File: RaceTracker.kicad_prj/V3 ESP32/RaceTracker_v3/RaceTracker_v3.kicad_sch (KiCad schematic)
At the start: 44 parts, among them J1 USB-C, J2 Battery, J3 Qwiic GPS (I2C), J4 microSD, J5 UART Debug, SW1 PWR, SW2 RESET, SW3 BOOT, U1 ESP32-S3-WROOM-1-N8, U2 MCP73831T-2ACI/OT, U3 AP2112K-3.3, U4 WSEN-ISDS

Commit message: V3: manuelle Schaltplan-Aenderungen committen
Co-Authored-By: Claude Sonnet 5 <noreply@anthropic.com>
Claude-Session: https://claude.ai/code/session_01KJ1x8W8LsYuDo52VfB14br
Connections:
- net GND: now also R1.1, R2.1; no longer R1.2, R2.2
- net at J1.B5 (CC2): now also R2.2; no longer R2.1
- net at J1.A5 (CC1): now also R1.2; no longer R1.1
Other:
- moved on the sheet: C1, C10, C2, C3, C4, C5, C6, C7, C8, C9, D2, D3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

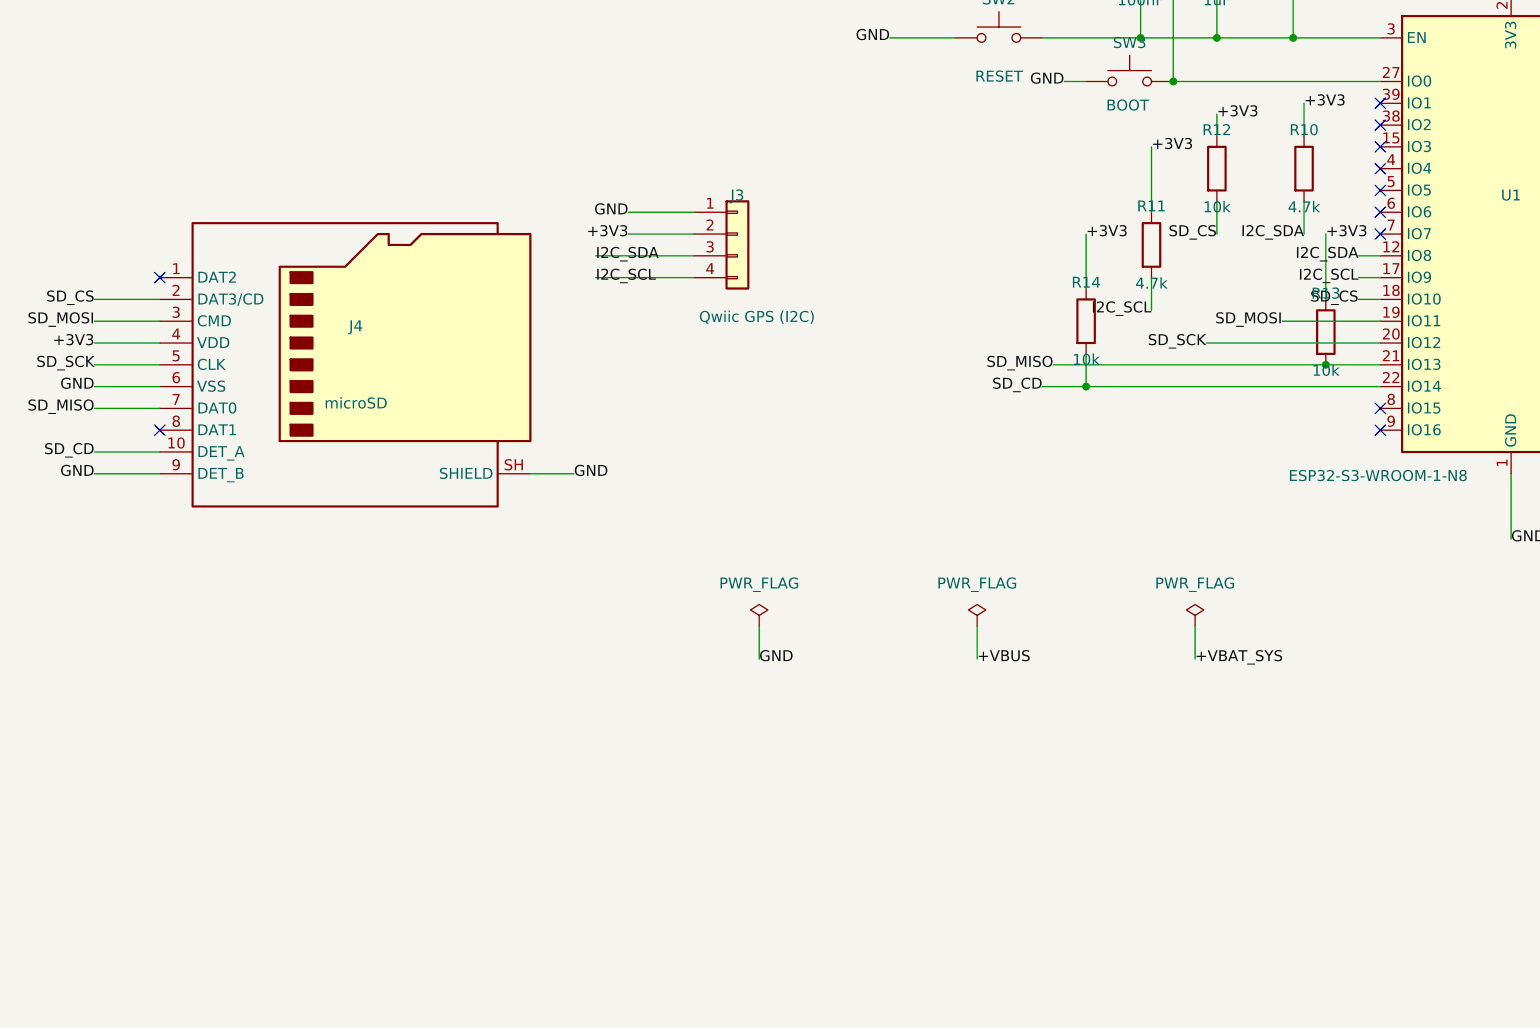
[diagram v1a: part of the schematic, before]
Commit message: V3: e-Paper Connector-Header (J6) ergaenzt
Co-Authored-By: Claude Sonnet 5 <noreply@anthropic.com>
Claude-Session: https://claude.ai/code/session_01KJ1x8W8LsYuDo52VfB14br
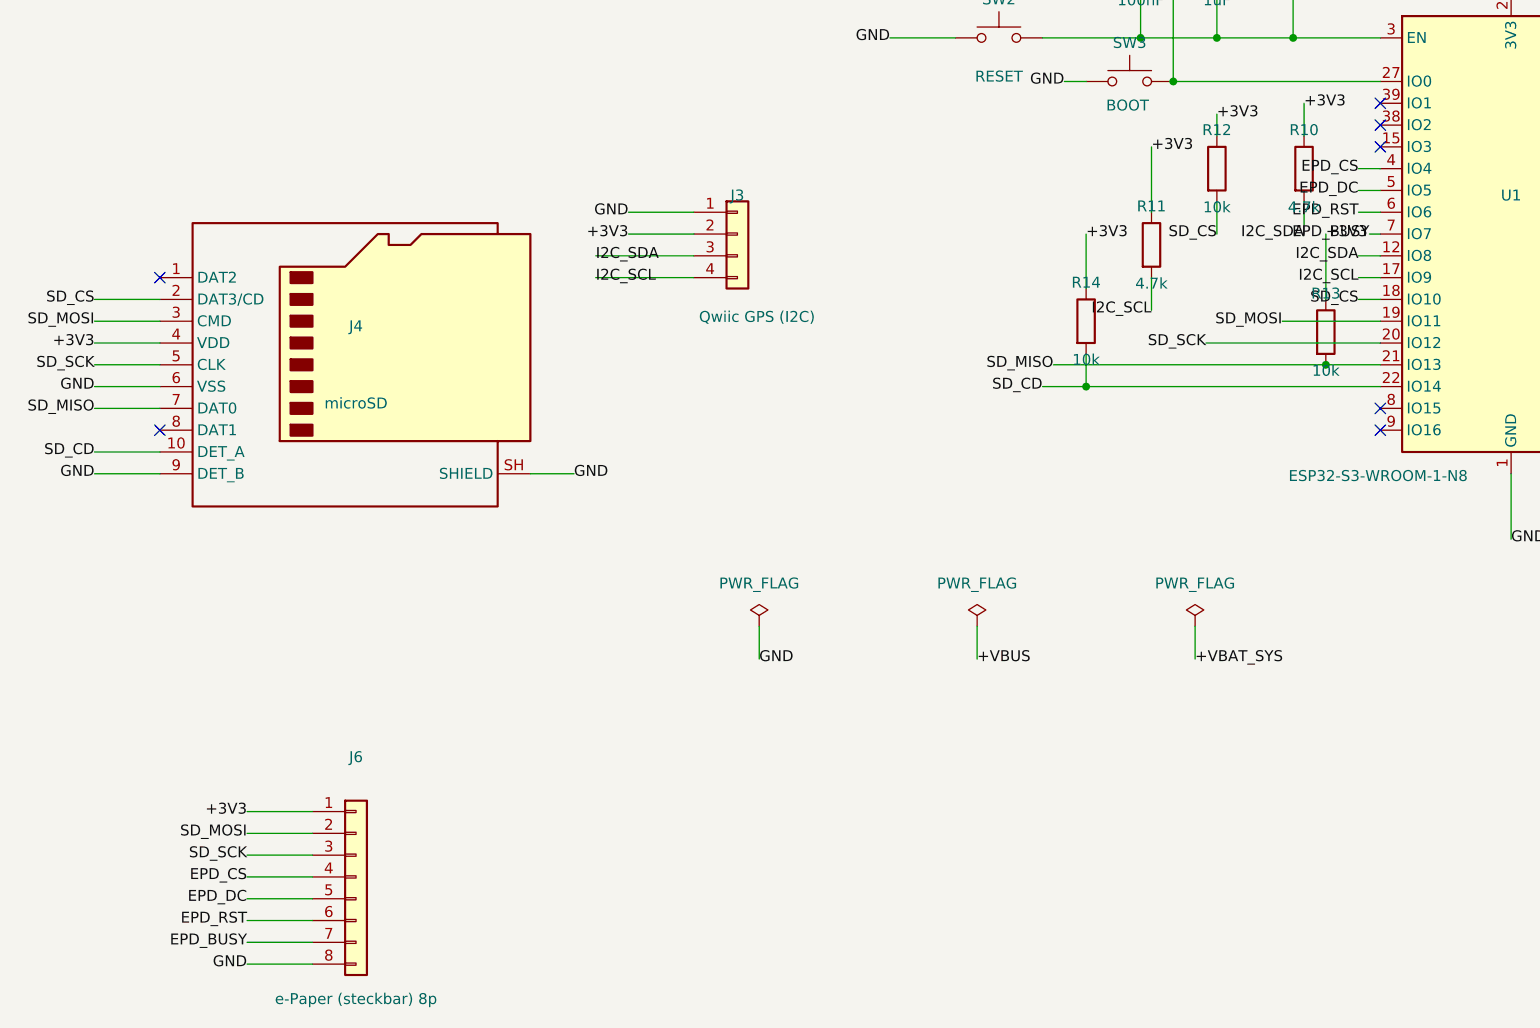
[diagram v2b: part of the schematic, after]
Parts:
- added J6: e-Paper (steckbar) 8p, Connector_PinHeader_2.54mm:PinHeader_1x08_P2.54mm_Vertical, symbol Connector_Generic:Conn_01x08
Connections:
- net +3V3: now also J6.1 (Pin_1)
- net GND: now also J6.8 (Pin_8)
- net SD_MOSI: now also J6.2 (Pin_2)
- net SD_SCK: now also J6.3 (Pin_3)
- net EPD_CS: now reaches U1.4 (IO4)
- net EPD_CS: now also J6.4 (Pin_4)
- net EPD_DC: now reaches U1.5 (IO5)
- net EPD_DC: now also J6.5 (Pin_5)
- net EPD_RST: now reaches U1.6 (IO6)
- net EPD_RST: now also J6.6 (Pin_6)
- net EPD_BUSY: now reaches U1.7 (IO7)
- net EPD_BUSY: now also J6.7 (Pin_7)
- no-connect marks 31 -> 27

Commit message: V3: C8-Plane-Via, J3 zur Steckerleiste, Pin-Beschriftung
- C8: fehlenden /+3V3-Stitching-Via ergaenzt (GND-Pad hatte schon einen
  passenden Via in Reichweite, kein neuer noetig)
- J3 (Qwiic GPS I2C) von JST-SH auf 2.54mm-Stiftleiste
  (PinHeader_1x04_P2.54mm_Vertical) umgestellt - das reale SparkFun-
  Modul hat dafuer eine eigene PTH-Stiftleiste mit identischer
  Pinbelegung (GND/VCC/SDA/SCL), verifiziert gegen das Datenblatt im
  Repo-Root. Schaltplan-Footprint-Feld + PCB-Footprint getauscht,
  Position/Netze erhalten. Feinplatzierung macht der User selbst.
- Pin-Funktions-Beschriftung (Silk) fuer alle 3 Stiftleisten-Header
  J3/J5/J6 ergaenzt (GND/3V3/SDA/SCL, RXD/TXD, 3V3/MOSI/SCK/CS/DC/
  RST/BUSY/GND), 0.8mm Texthoehe, damit beim Verkabeln nichts
  vertauscht wird

Verifiziert: kicad-cli pcb drc --severity-all -> 0 Errors (nur 5
erwartete lib_footprint_mismatch-Warnings + 4 via_dangling/2
unconnected von J3s alter JST-Position, die der User beim
Neuplatzieren mit aufraeumt). ERC weiterhin 0/0.

Co-Authored-By: Claude Sonnet 5 <noreply@anthropic.com>
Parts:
- J3: footprint Connector_JST:JST_SH_SM04B-SRSS-TB_1x04-1MP_P1.00mm_Horizontal -> Connector_PinHeader_2.54mm:PinHeader_1x04_P2.54mm_Vertical
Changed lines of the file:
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@@
 			)
 		)
-		(property "Footprint" "Connector_JST:JST_SH_SM04B-SRSS-TB_1x04-1MP_P1.00mm_Horizontal"
+		(property "Footprint" "Connector_PinHeader_2.54mm:PinHeader_1x04_P2.54mm_Vertical"
 			(at 139.7 149.86 0)
 			(hide yes)

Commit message: V3: MPN/Manufacturer/LCSC fuer alle 44 Bauteile ergaenzt
- Alle Passiva (R/C) auf gut verfuegbare, guenstige JLCPCB-Basic-Parts
  gesetzt (Uniroyal Elec Widerstaende, Samsung/Yageo Kondensatoren)
- U1 ESP32-S3-WROOM-1-N8 exakter LCSC-Treffer (C2913198)
- U4 WSEN-ISDS: nicht bei LCSC gelistet, DigiKey-Verfuegbarkeit
  dokumentiert (574 Stk, $9.35@1)
- D2/D3 LED-Farben (Rot/Gruen) angenommen - im Schaltplan nicht
  spezifiziert, User sollte pruefen
- SW1 MPN nicht gegen exakte Footprint-Masse verifizierbar - vor
  Bestellung Datenblatt pruefen
- BOM-CSV nach bom/bom.csv exportiert

Quelle: jlcsearch.tscircuit.com (kostenlose LCSC-API, kein Key noetig)
+ DigiKey-Produktseite fuer den einen nicht bei LCSC gefuehrten Teil.

Co-Authored-By: Claude Sonnet 5 <noreply@anthropic.com>
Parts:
- C1, C4, C5, C9: LCSC (none) -> C15849; MPN (none) -> CL10A105KB8NNNC; Manufacturer (none) -> Samsung Electro-Mechanics
- C10, C11, C12, C6, C8: LCSC (none) -> C14663; MPN (none) -> CC0603KRX7R9BB104; Manufacturer (none) -> Yageo
- C13: LCSC (none) -> C15850; MPN (none) -> CL21A106KAYNNNE; Manufacturer (none) -> Samsung Electro-Mechanics
- C2, C3: LCSC (none) -> C19666; MPN (none) -> CL10A475KO8NNNC; Manufacturer (none) -> Samsung Electro-Mechanics
- C7: LCSC (none) -> C45783; MPN (none) -> CL21A226MAQNNNE; Manufacturer (none) -> Samsung Electro-Mechanics
- D1: LCSC (none) -> C2687116; MPN (none) -> USBLC6-2SC6; Manufacturer (none) -> STMicroelectronics
- D2: LCSC (none) -> C965799; MPN (none) -> XL-1608SURC-06; Manufacturer (none) -> XLSEMI (Chenzhixin)
- D3: LCSC (none) -> C965804; MPN (none) -> XL-1608UGC-04; Manufacturer (none) -> XLSEMI (Chenzhixin)
- D4: LCSC (none) -> C85402; MPN (none) -> PESD5V0S1UL; Manufacturer (none) -> Nexperia
- J1: LCSC (none) -> C165948; MPN (none) -> TYPE-C-31-M-12; Manufacturer (none) -> Korean Hroparts Elec
- J2: LCSC (none) -> C295747; MPN (none) -> S2B-PH-SM4-TB(LF)(SN); Manufacturer (none) -> JST
- J3, J5: LCSC (none) -> C2691448; MPN (none) -> PZ254V-11-04P; Manufacturer (none) -> BOOMELE
- J4: LCSC (none) -> C585350; MPN (none) -> 104031-0811; Manufacturer (none) -> Molex
- J6: LCSC (none) -> C492407; MPN (none) -> PZ254V-11-08P; Manufacturer (none) -> BOOMELE
- R1, R2: LCSC (none) -> C23186; MPN (none) -> 0603WAF5101T5E; Manufacturer (none) -> Uniroyal Elec
- R10, R11: LCSC (none) -> C23162; MPN (none) -> 0603WAF4701T5E; Manufacturer (none) -> Uniroyal Elec
- R12, R13, R14, R15, R8, R9: LCSC (none) -> C25804; MPN (none) -> 0603WAF1002T5E; Manufacturer (none) -> Uniroyal Elec
- R3: LCSC (none) -> C22975; MPN (none) -> 0603WAF2001T5E; Manufacturer (none) -> Uniroyal Elec
- R4, R5: LCSC (none) -> C21190; MPN (none) -> 0603WAF1001T5E; Manufacturer (none) -> Uniroyal Elec
- R6, R7: LCSC (none) -> C22935; MPN (none) -> 0603WAF1004T5E; Manufacturer (none) -> Uniroyal Elec
- SW1: LCSC (none) -> C126888; MPN (none) -> DSWB01LHGET; Manufacturer (none) -> DECIGN
- SW2, SW3: LCSC (none) -> C231329; MPN (none) -> B3U-1000P; Manufacturer (none) -> Omron
- U1: LCSC (none) -> C2913198; MPN (none) -> ESP32-S3-WROOM-1-N8; Manufacturer (none) -> Espressif Systems
- U2: LCSC (none) -> C424093; MPN (none) -> MCP73831T-2ACI/OT; Manufacturer (none) -> Microchip Technology
- U3: LCSC (none) -> C23380830; MPN (none) -> AP2112K-3.3TRG1; Manufacturer (none) -> Diodes Incorporated
- U4: MPN (none) -> 2536030320001; Manufacturer (none) -> Wuerth Elektronik
